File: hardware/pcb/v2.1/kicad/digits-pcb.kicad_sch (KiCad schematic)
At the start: 45 parts, among them J1 Conn_02x20_Odd_Even, J3 VIN_BARREL_PIGTAIL, J4 Conn_01x07, J6 Conn_01x02, J7 Screw_Terminal_01x02, J8 Conn_01x04, J9 Conn_01x03, SW1 SW_Push, U1 LM2596S-5, U3 RP2040, U4 W25Q16JVSSIQ, U5 AMS1117-3.3, Y1 ABM8-272-T3

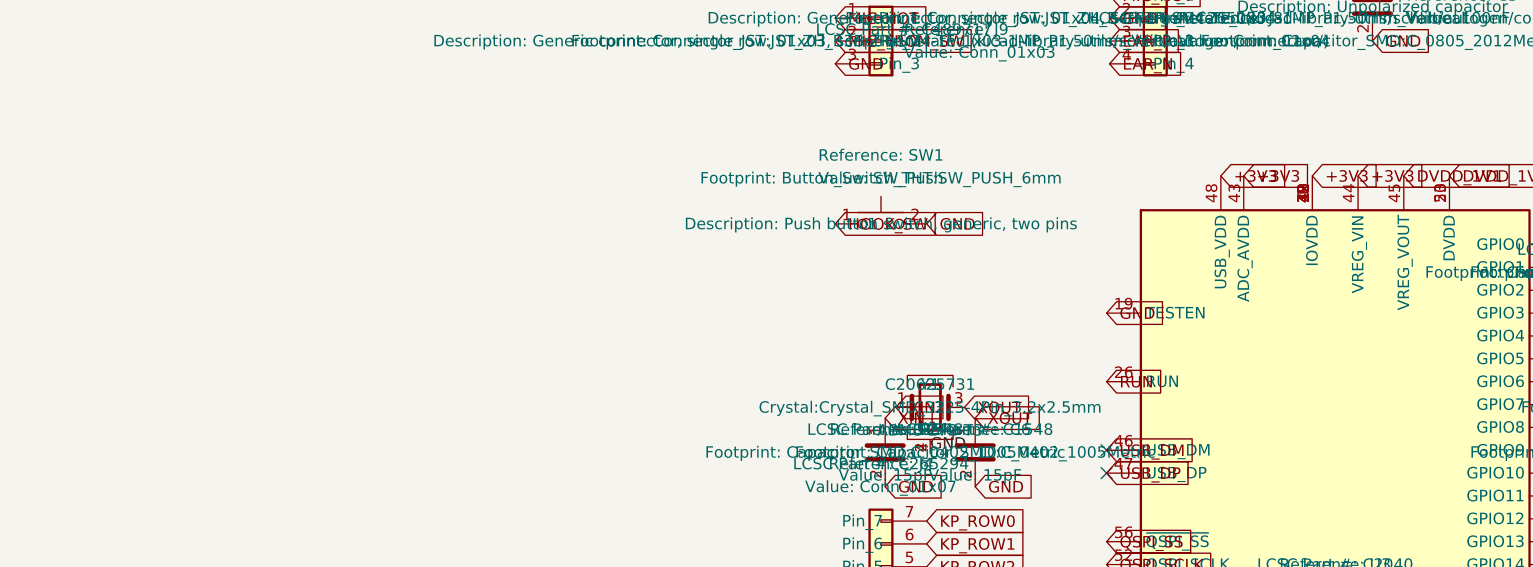
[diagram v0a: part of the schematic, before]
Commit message: feat(hardware): add BOOTSEL button (SW2) to V2.1 schematic
V2 has no BOOTSEL button, which makes first-flash and recovery
require manually shorting U4 pin 1 (QSPI_SS) to GND with a paperclip
while powering on. During V2 bring-up that procedure killed one
RP2040's SWD interface when a slipped wire shorted +3.3 V to GND
through the polyswitch. ERRATA item 4 in hardware/pcb/v2/ERRATA.md
prescribes the fix.

SW2 is a 6 mm THT tact switch (Switch:SW_Push, footprint
Button_Switch_THT:SW_PUSH_6mm, same part as SW1 hookswitch) wired
QSPI_SS to GND. Pressing it during power-on drags QSPI_SS low in the
bootrom's flash-CS sample window and the RP2040 enters BOOTSEL (USB
MSC + PICOBOOT) until the next reset. Standard Pi Pico practice.

Schematic only. PCB layout placement of SW2 is a follow-up edit on
the .kicad_pcb file and is not in this commit.

Verification:
  kicad-cli sch erc digits-pcb.kicad_sch -> 0 errors, 0 warnings
  Netlist QSPI_SS now has 3 nodes: U3.56, U4.1, SW2.1 (was 2).
  Netlist GND gains SW2.2.
  BOM gains SW2 row with the SW_PUSH_6mm footprint.
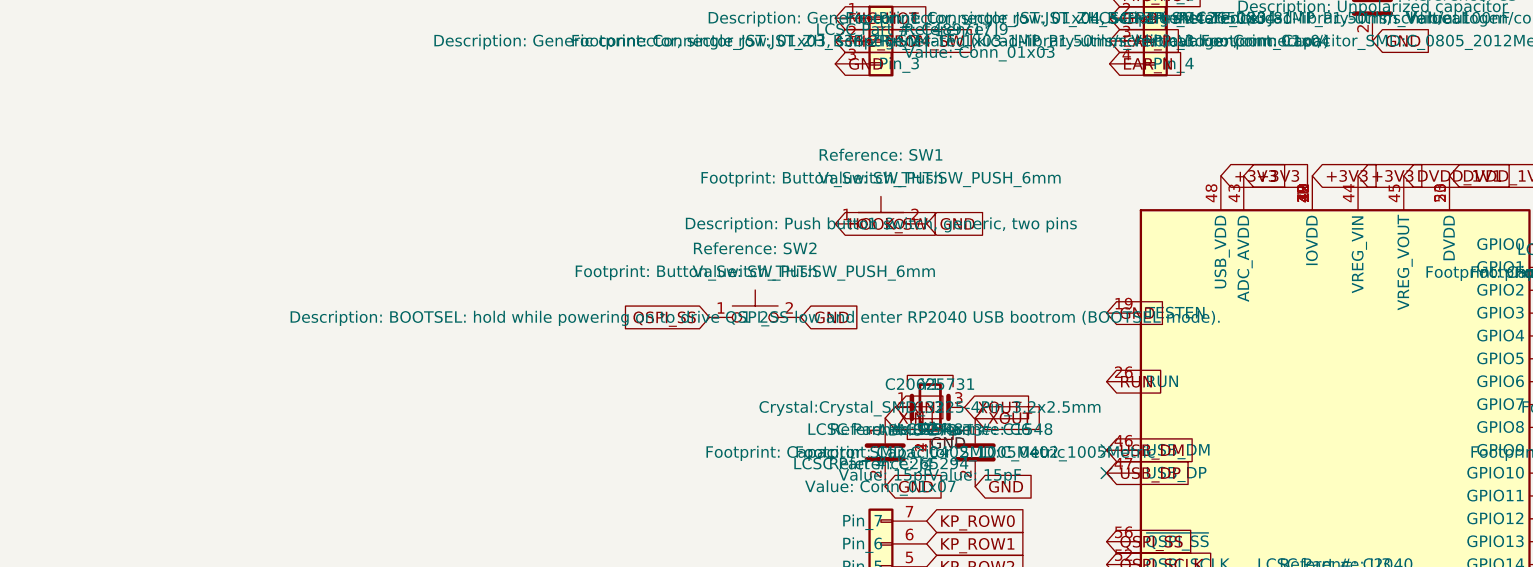
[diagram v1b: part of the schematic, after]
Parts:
- added SW2: SW_Push, Button_Switch_THT:SW_PUSH_6mm, symbol Switch:SW_Push
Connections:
- net GND: now also SW2.2
- net QSPI_SS: now also SW2.1
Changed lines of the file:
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@@
+    )
+  )
+  (global_label "QSPI_SS" (shape input) (at 30.48 65 180)
+    (effects (font (size 1.27 1.27)) (justify right))
+    (property "Intersheetrefs" "${INTERSHEET_REFS}" (at 30.48 65 180) (show_name)
+      (effects (font (size 1.27 1.27)))
+    )
+  )
+  (global_label "GND" (shape input) (at 40.64 65 0)
+    (effects (font (size 1.27 1.27)) (justify left))
+    (property "Intersheetrefs" "${INTERSHEET_REFS}" (at 40.64 65 0) (show_name)
+      (effects (font (size 1.27 1.27)))
     )
   )
@@
         )
       )
+    )
+  )
+  (symbol (lib_id "Switch:SW_Push") (at 35.56 65 0) (unit 1)
+    (in_bom yes) (on_board yes) (dnp no) (fields_autoplaced)
+    (property "Reference" "SW2" (at 35.56 57.38 0) (show_name)
+      (effects (font (size 1.27 1.27)))
+    )
+    (property "Value" "SW_Push" (at 35.56 59.92 0) (show_name)
+      (effects (font (size 1.27 1.27)))
+    )
+    (property "Footprint" "Button_Switch_THT:SW_PUSH_6mm" (at 35.56 59.92 0) (show_name)
+      (effects (font (size 1.27 1.27)))
+    )
+    (property "Datasheet" "" (at 35.56 59.92 0) (show_name)
+      (effects (font (size 1.27 1.27)))
+    )
+    (property "Description" "BOOTSEL: hold while powering on to drive QSPI_SS low and enter RP2040 USB bootrom (BOOTSEL mode)." (at 35.56 65 0) (show_name)
+      (effects (font (size 1.27 1.27)))
+    )
+    (property "LCSC Part #" "" (at 35.56 57.38 0) (show_name)
+      (effects (font (size 1.27 1.27)))
+    )
+    (pin "1")
+    (pin "2")
+    (instances
+      (project "digits-pcb"
+        (path "/74ec24e7-a8af-4132-928f-b03228b07139"
+          (reference "SW2") (unit 1)
+        )
+      )

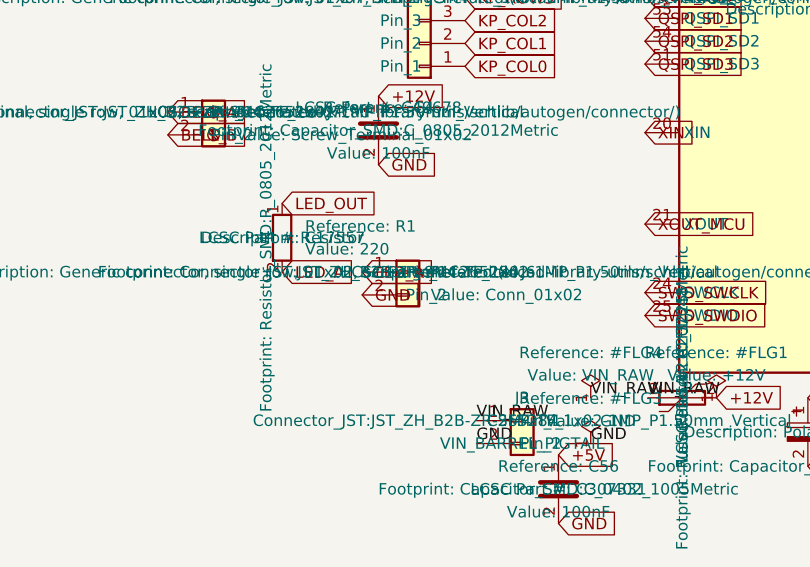
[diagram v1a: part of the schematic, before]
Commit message: fix(hardware): swap J6 LED polarity and place SW2 on PCB v2.1 (#322)
J6 pin 1 and pin 2 net assignments are swapped so the stock donor-phone
LED cable plugs in directly without per-unit crimp rework. Pin 1 is now
GND, pin 2 is LED_A. See hardware/pcb/v2/ERRATA.md section 8 for the
underlying defect.

SW2 (BOOTSEL tact switch) was already in the v2.1 schematic but had no
PCB placement. Placed on the carrier with QSPI_SS and GND routed clean,
labeled BOOTSEL on the silkscreen.

DRC: 0 errors, 0 unconnected items. Remaining warnings are pre-existing
silkscreen overlap and library-footprint drift carried over from main.
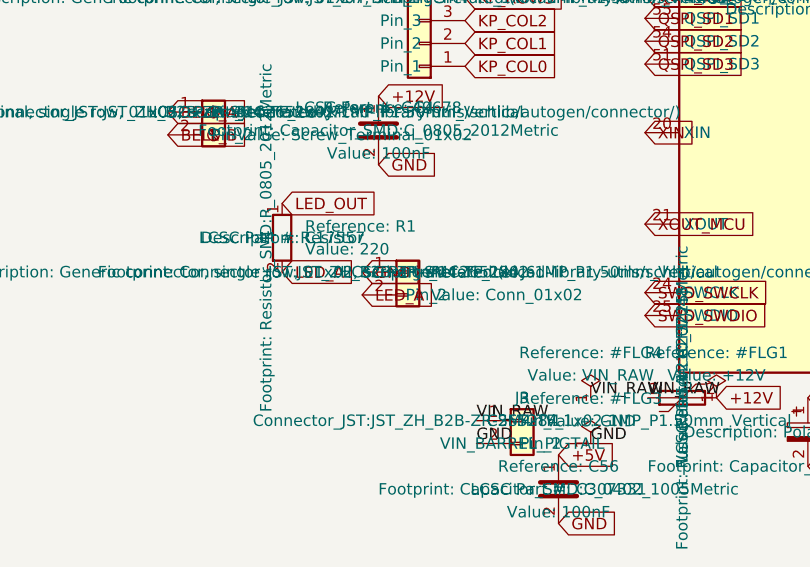
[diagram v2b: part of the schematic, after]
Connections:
- net GND: now also J6.1 (Pin_1); no longer J6.2 (Pin_2)
- net LED_A: now also J6.2 (Pin_2); no longer J6.1 (Pin_1)
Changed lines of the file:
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@@
     )
   )
-  (global_label "LED_A" (shape input) (at 43.18 125.73 0)
+  (global_label "LED_A" (shape input) (at 43.18 128.27 0)
     (effects (font (size 1.27 1.27)) (justify left))
-    (property "Intersheetrefs" "${INTERSHEET_REFS}" (at 43.18 125.73 0) (show_name)
+    (property "Intersheetrefs" "${INTERSHEET_REFS}" (at 43.18 128.27 0) (show_name)
       (effects (font (size 1.27 1.27)))
     )
@@
     )
   )
-  (global_label "GND" (shape input) (at 43.18 128.27 0)
+  (global_label "GND" (shape input) (at 43.18 125.73 0)
     (effects (font (size 1.27 1.27)) (justify left))
-    (property "Intersheetrefs" "${INTERSHEET_REFS}" (at 43.18 128.27 0) (show_name)
+    (property "Intersheetrefs" "${INTERSHEET_REFS}" (at 43.18 125.73 0) (show_name)
       (effects (font (size 1.27 1.27)))
     )

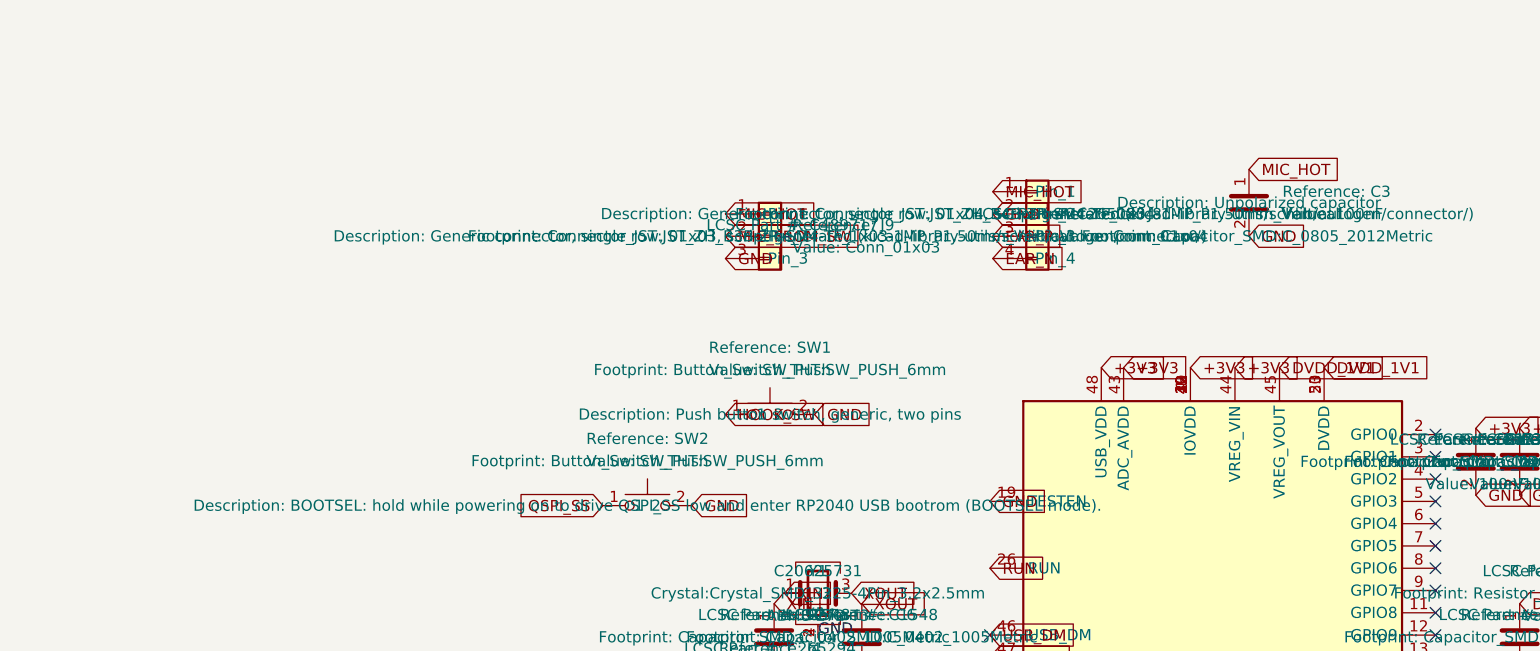
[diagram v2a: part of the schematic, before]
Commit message: feat(hardware): integrate DPDT hook switch and on-board boost converter into PCB v2.1
Two architectural changes consolidated into v2.1 (previously scoped for v3):

1. DPDT hook switch replaces SW1 (tact switch) and J9 (mic kill JST connector).
   Single 6-pin telephone hook switch (IL Switch 2240 / Innocent INH-2240 family)
   provides both hook sense and mic kill from one mechanical actuation. Lifting
   the handset both signals off-hook and connects the microphone to the codec.
   Eliminates J9 connector and its external microswitch harness.

2. XL6019 boost converter (12V to 42V) replaces the external mains transformer.
   Feeds the DRV8871 H-bridge VM pin so the bell sees 84Vpp drive instead of
   24Vpp. At ~4k coil impedance the bell ringer gets ~12x the power of direct
   12V drive, roughly halfway to transformer-level loudness on the perceptual
   scale. Eliminates the external 120V/12V transformer and its flying wires.
   J7 stays as the bell coil output.

Components added:
- SW1: SW_DPDT_x2 with custom 24.2x17.1mm footprint (5mm pin pitch, 7.75mm
  row spacing, 0.9mm signal pin / 2.1mm mounting pin)
- U10: XLSEMI XL6019E1 boost IC (LCSC C73018, TO-263-5)
- L10: 47uH/4.6A shielded power inductor (LCSC C9906, 12.3x12.3mm)
- D10: SS56 60V/5A Schottky diode (LCSC C65009, SMA)
- C100: 100uF/63V SMD electrolytic output cap (LCSC C28241, 10mm dia)
- C101: 1uF/100V 0805 ceramic output cap
- R20/R21: 64.9k/2k 0402 feedback divider (sets VBOOST to 41.8V)

Components removed:
- SW1 (2-pin 6mm tact switch)
- J9 (3-pin JST ZH mic kill connector)

LCSC-sourced symbols and footprints pulled via easyeda2kicad, registered
through sym-lib-table and fp-lib-table.

Schematic notes:
- VBOOST is a local net in the ringer sub-sheet; PWR_FLAG marks it as driven
- LCSC XL6019 symbol mislabels pin 6 (thermal tab) as SW; overridden with GND
  label in schematic to match the datasheet
- New refs (U10, L10, D10, C100, C101, R20, R21) chosen to avoid collisions
  with existing parent-sh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
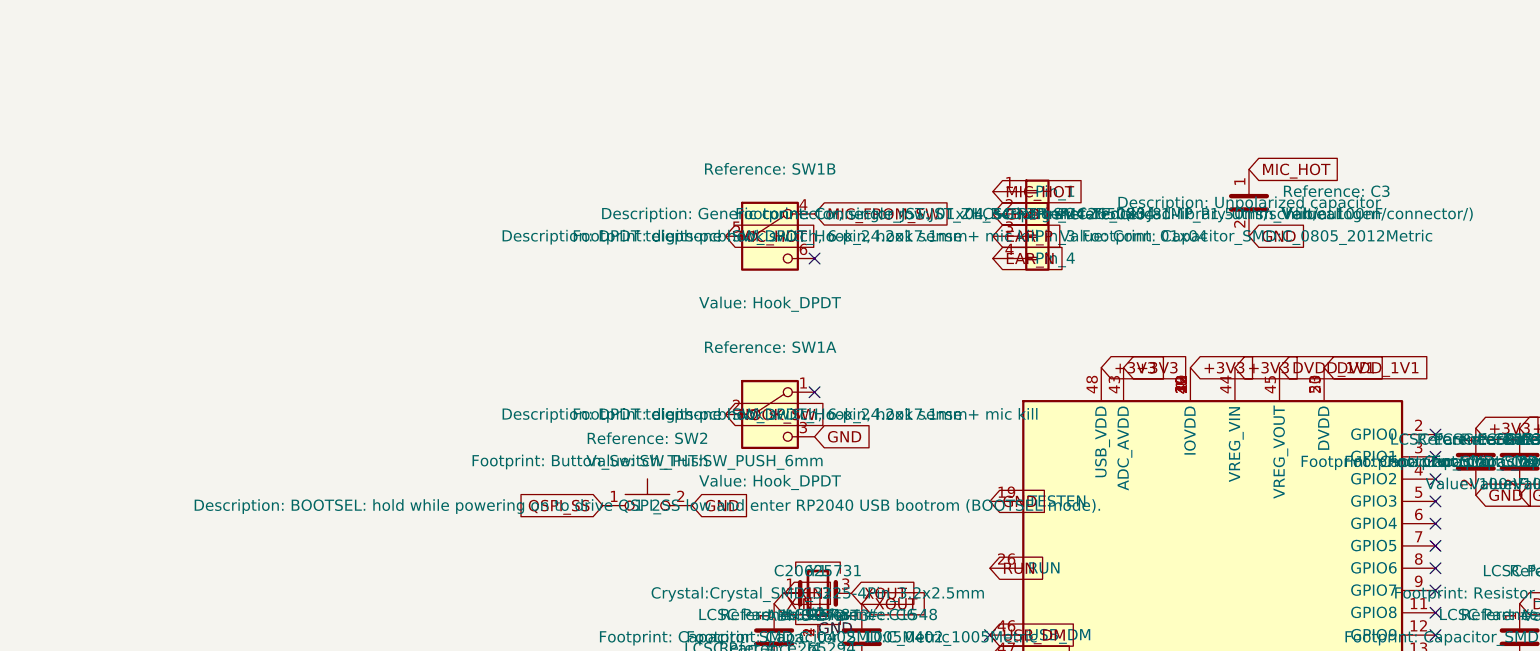
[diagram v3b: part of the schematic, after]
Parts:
- removed J9: Conn_01x03, Connector_JST:JST_ZH_B3B-ZR-SM4-TF_1x03-1MP_P1.50mm_Vertical, symbol Connector_Generic:Conn_01x03
- added unit 2 of SW1
- SW1: value SW_Push -> Hook_DPDT; footprint Button_Switch_THT:SW_PUSH_6mm -> digits-pcb:SW_DPDT_Hook_24.2x17.1mm; symbol Switch:SW_Push -> Switch:SW_DPDT_x2
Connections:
- net GND: now also SW1.3 (C); no longer SW1.2
- net HOOK_SW: now also SW1.2 (B); no longer SW1.1
- net MIC_FROM_SW: now also SW1.4 (A)
- net MIC_HOT: now also SW1.5 (B)
- no-connect marks 37 -> 39

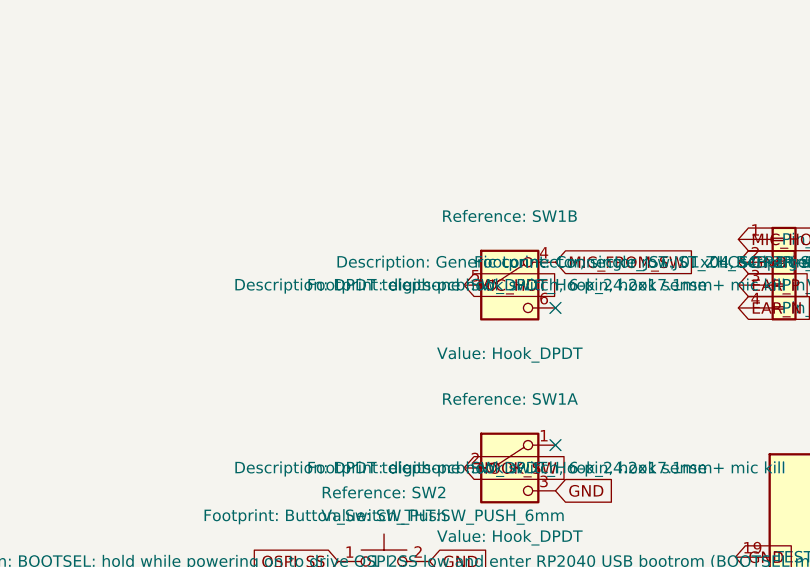
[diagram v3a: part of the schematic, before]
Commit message: fix(hardware): move C54/C55 to VBOOST, add power indicator LEDs, drop unused mounting pin holes
Three follow-ups from the V2.1 schematic review:

1. C54 (100nF HF) and C55 (47uF bulk) were the DRV8871 VM decoupling caps in
   V2 when VM sat on +12V. The earlier boost converter integration moved
   DRV8871 VM to VBOOST but left these caps on +12V, leaving U2 pin 5 with
   zero local decoupling. C100/C101 (the boost output caps) were doing the
   work from across the board.

   Fix: move C54 and C55 to VBOOST. They now serve as close-in VM decoupling
   for the DRV8871. C100/C101 stay as the boost output filter near U10.

2. Add D2/R12 (red LED, 1k) on +12V and D3/R13 (green LED, 330R) on +3V3.
   D2 lights when board power is present, D3 lights when the downstream
   regulator tree (LM2596 -> AMS1117) is working. Quick visual sanity check
   without a multimeter.

3. Drop the two NPTH mounting pin holes from the DPDT hook switch footprint.
   The 24x17 generic clones (per teardown of the original Sangyn ringer
   board) do not populate the locating pins; the switch is held by the six
   signal pins plus phone-body pressure.

ERC clean. Netlist confirms VBOOST = {C54.1, C55.1, C100.1, C101.1, D10.1,
R20.1, U2.5}.
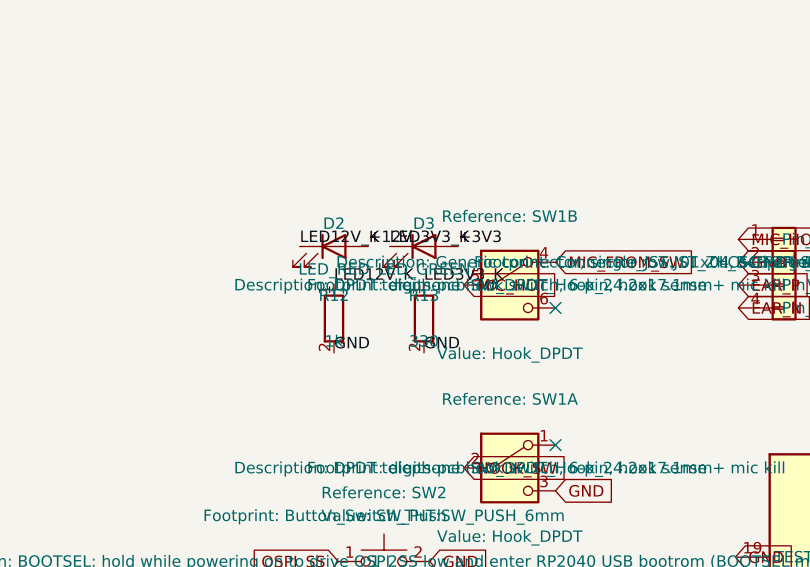
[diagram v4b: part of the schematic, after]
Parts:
- added D2: LED_RED, LED_SMD:LED_0603_1608Metric, symbol Device:LED
- added D3: LED_GREEN, LED_SMD:LED_0603_1608Metric, symbol Device:LED
- added R12: 1k, Resistor_SMD:R_0402_1005Metric, symbol Device:R
- added R13: 330, Resistor_SMD:R_0402_1005Metric, symbol Device:R
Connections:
- net +12V: now also D2.2 (A)
- net +3V3: now also D3.2 (A)
- net GND: now also R12.2, R13.2
- new net LED12V_K: D2.1 (K), R12.1
- new net LED3V3_K: D3.1 (K), R13.1
